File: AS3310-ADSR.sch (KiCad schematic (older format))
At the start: 51 parts

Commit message: Add Eurocad symbols and footprints.
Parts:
- added C? (x2): 10uF, symbol Device:C
- added J?: EURO_PWR_2x5, symbol eurorack:EURO_PWR_2x5
- added J?: ENVELOPE_OUT, symbol Connector:AudioJack2_Ground_SwitchT
- added TP?: GATE_IN, symbol Connector:TestPoint
- added TP?: TRIGGER_IN, symbol Connector:TestPoint
- added TP?: ENVELOPE_OUT, symbol Connector:TestPoint
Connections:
- net labels removed: ENVELOPE_OUT
- wire segments 123 -> 139
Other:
- note added: "Auto"
- note added: "Damp"
- note added: "Normal"
- moved on the sheet: C?, R?, U?

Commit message: Refactor
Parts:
- removed J?: EURO_PWR_2x5, symbol eurorack:EURO_PWR_2x5
- added C11, C8: .1uF, Seattle_Synths:C_Disc_D7.5mm_W2.5mm_P5.00mm, symbol Device:C
- added J2: EURO_PWR_2x5, Seattle_Synths:PinHeader_2x05_P2.54mm_Vertical, symbol Eurocad:EURO_PWR_2x5
- added unit 3 of U1
- C1, C10, C2, C3, C4, C5, C6, C7, C9: renamed from C?; footprint (none) -> Seattle_Synths:C_Disc_D7.5mm_W2.5mm_P5.00mm
- D1, D2: renamed from D?; footprint (none) -> Seattle_Synths:D_DO-35_SOD27_P7.62mm_Horizontal
- J1, J3, J4: renamed from J?; footprint (none) -> Seattle_Synths:Jack_3.5mm_QingPu_WQP-PJ398SM_Vertical_CircularHoles
- R1, R10, R11, R12, R13, R14, R15, R16, R17, R18, R19, R2, R20, R21, R22, R23, R24, R25, R3, R4, R5, R6, R7, R8, R9: renamed from R?; footprint (none) -> Seattle_Synths:R_Axial_DIN0207_L6.3mm_D2.5mm_P10.16mm_Horizontal
- RV1, RV2, RV3, RV4: renamed from RV?; footprint (none) -> Seattle_Synths:Potentiometer_Alpha_RD901F-40-00D_Single_Vertical
- RV5, RV6: renamed from RV?; footprint (none) -> Seattle_Synths:Potentiometer_Runtron_RM-065_Vertical
- SW2: renamed from SW?; footprint (none) -> Seattle_Synths:SW_PUSH_6mm_H5mm
- TP1, TP2, TP3: renamed from TP?; footprint (none) -> Seattle_Synths:TestPoint_Pad_4.0x4.0mm
- U1, U3, U4: renamed from U?; footprint (none) -> Seattle_Synths:DIP-8_W7.62mm
- U2: renamed from U?; footprint (none) -> Seattle_Synths:DIP-16_W7.62mm
- gave numbers to parts that had none: 3
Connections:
- wire segments 139 -> 141
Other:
- moved on the sheet: C10, C9

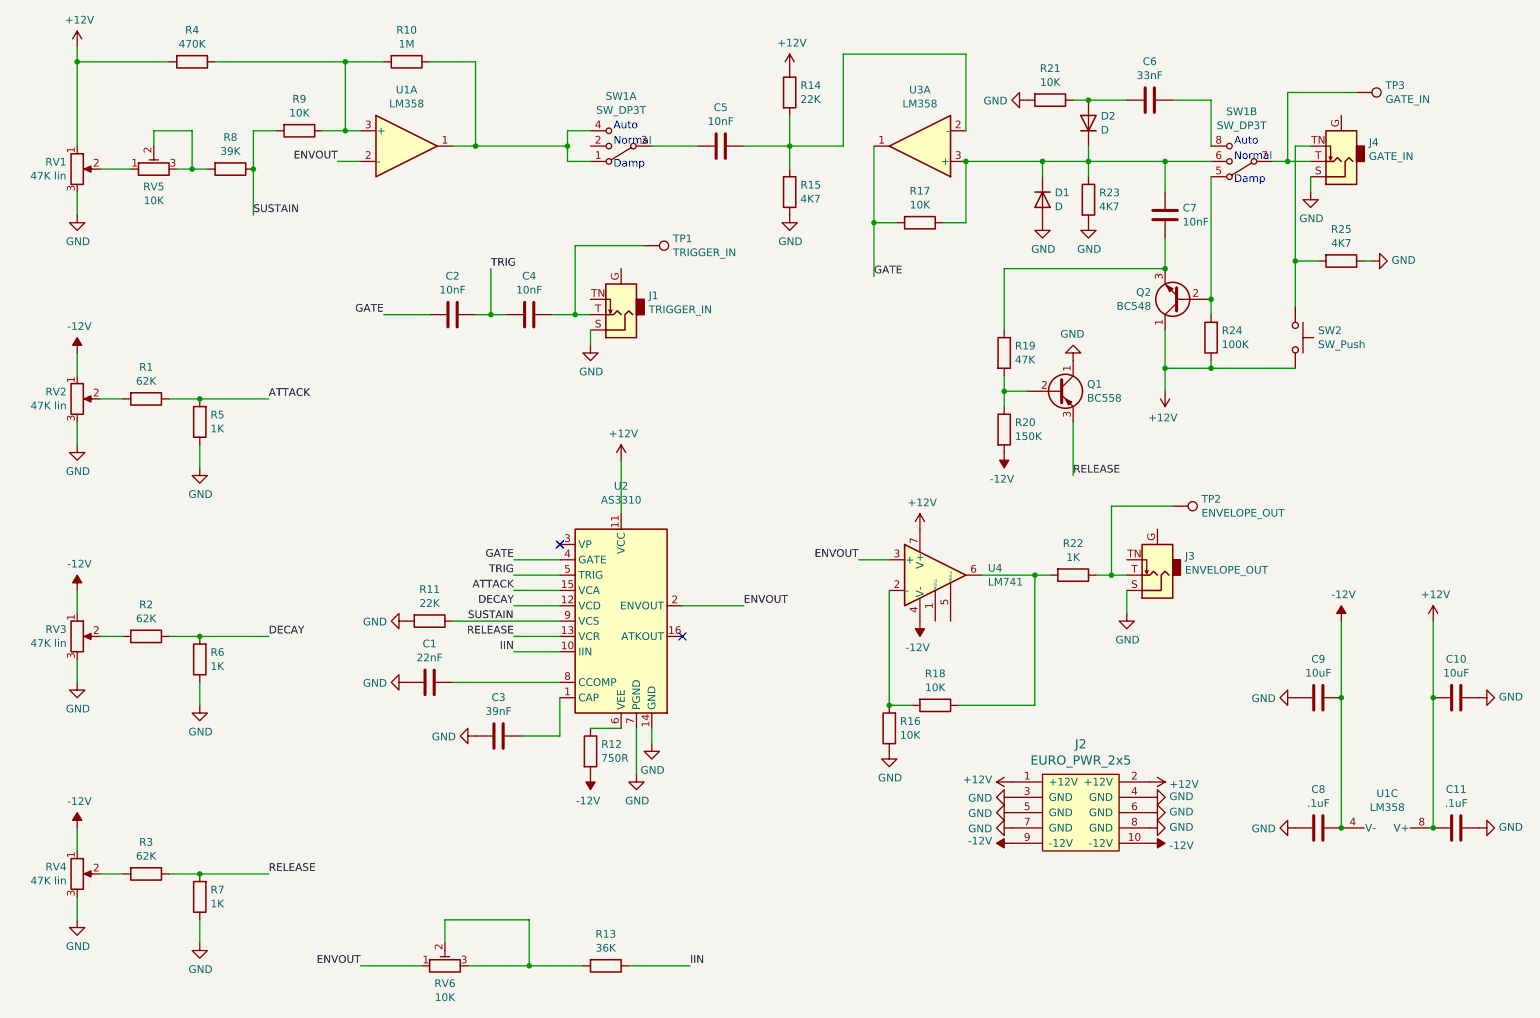
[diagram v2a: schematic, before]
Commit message: Refactor DP3T switch.
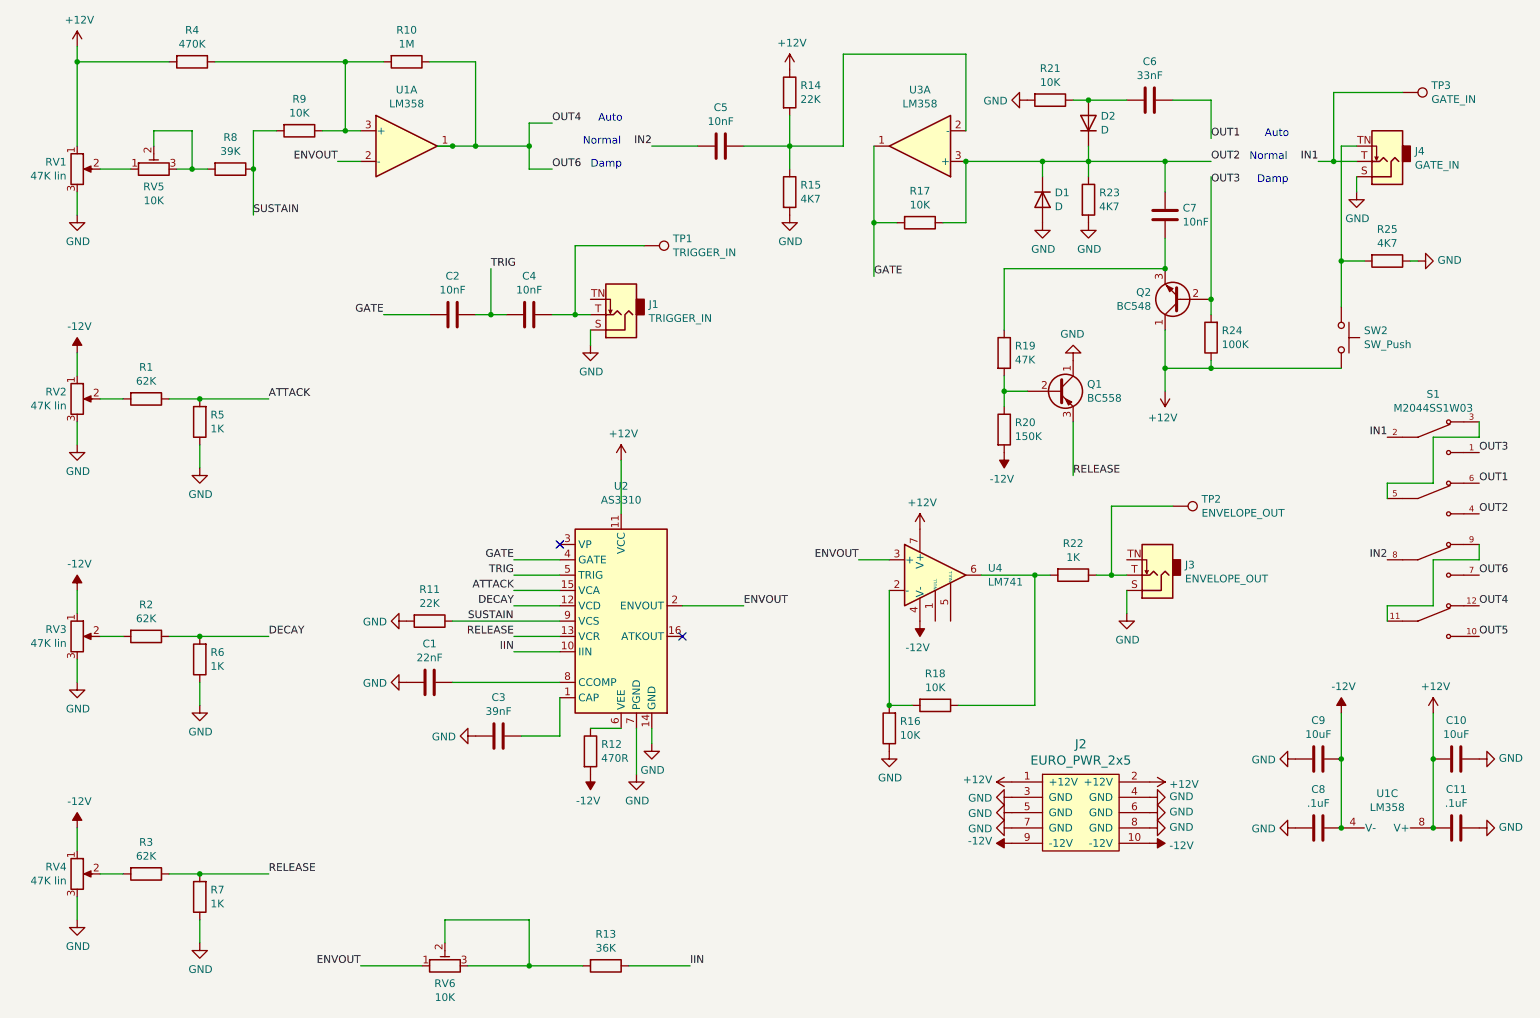
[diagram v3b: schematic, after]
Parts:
- removed J1: TRIGGER_IN, Seattle_Synths:Jack_3.5mm_QingPu_WQP-PJ398SM_Vertical_CircularHoles, symbol Connector:AudioJack2_Ground_SwitchT
- removed J3: ENVELOPE_OUT, Seattle_Synths:Jack_3.5mm_QingPu_WQP-PJ398SM_Vertical_CircularHoles, symbol Connector:AudioJack2_Ground_SwitchT
- removed J4: GATE_IN, Seattle_Synths:Jack_3.5mm_QingPu_WQP-PJ398SM_Vertical_CircularHoles, symbol Connector:AudioJack2_Ground_SwitchT
- removed SW1: SW_DP3T, symbol Switch:SW_DP3T
- added J1: TRIGGER_IN, Seattle_Synths:Jack_3.5mm_QingPu_WQP-PJ398SM_Vertical_CircularHoles, symbol Connector:AudioJack2_SwitchT
- added J3: ENVELOPE_OUT, Seattle_Synths:CUI_MJ-63052A, symbol Connector:AudioJack2_SwitchT
- added J4: GATE_IN, Seattle_Synths:Jack_3.5mm_QingPu_WQP-PJ398SM_Vertical_CircularHoles, symbol Connector:AudioJack2_SwitchT
- added S1: M2044SS1W03, Seattle_Synths:SW_M2044SS1W03, symbol Seattle_Synths_DP3T_Switch:M2044SS1W03
- R12: value 750R -> 470R
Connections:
- net GND: now also J1.S, J3.S, J4.S
- net OUT4: now reaches R10.1, U1.1
- net OUT4: now also S1.12, S1.7
- net IN2: now reaches C5.2
- net IN2: now also S1.8
- net OUT2: now reaches C7.1, D1.1 (K), D2.1 (K), R17.1, R23.1, U3.3 (+)
- net OUT2: now also S1.4
- net OUT1: now reaches C6.1
- net OUT1: now also S1.6
- net OUT3: now reaches Q2.2 (B), R24.2
- net OUT3: now also S1.1
- net at R25.2, SW2.1: now also J4.TN
- net at R22.1, TP2.1: now also J3.T
- net IN1: now reaches TP3.1
- net IN1: now also J4.T, S1.2
- net at C4.1, TP1.1: now also J1.T
- new net: S1.11, S1.9
- new net: S1.3, S1.5
- new net OUT5: S1.10
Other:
- moved on the sheet: C10, C9, R25, SW2, TP3

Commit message: Refactor
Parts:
- removed S1: M2044SS1W03, Seattle_Synths:SW_M2044SS1W03, symbol Seattle_Synths_DP3T_Switch:M2044SS1W03
- added D3: LED, symbol Device:LED
- added R26: 330R, symbol Device:R
- added S1: M2044SS1W03, SW_M2044SS1W03, symbol Seattle_Synths:M2044SS1W03
- added TP4: -12V, symbol Connector:TestPoint
- added TP5: GND, symbol Connector:TestPoint
- added TP6: +12V, symbol Connector:TestPoint
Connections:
- net +12V: now also R26.2, TP6.1
- net -12V: now also TP4.1
- net GND: now also D3.1 (K), TP5.1
- net IN1: now also S1.2
- net IN2: now also S1.8
- net OUT1: now also S1.6
- net OUT2: now also S1.4
- net OUT3: now also S1.1
- net OUT4: now also S1.12, S1.7
- net OUT5: now also S1.10
- new net: S1.11, S1.9
- new net: S1.3, S1.5
- new net: D3.2 (A), R26.1
- no-connect marks 2 -> 7
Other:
- moved on the sheet: C10, C11, C3, C8, C9, U1C

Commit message: Refacctor
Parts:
- D3: footprint (none) -> Seattle_Synths:LED_D5.0mm
- J3: footprint Seattle_Synths:CUI_MJ-63052A -> Seattle_Synths:Jack_3.5mm_QingPu_WQP-PJ398SM_Vertical_CircularHoles
- R26: footprint (none) -> Seattle_Synths:R_Axial_DIN0207_L6.3mm_D2.5mm_P10.16mm_Horizontal
- S1: footprint SW_M2044SS1W03 -> Seattle_Synths:SW_M2044SS1W03
- TP4, TP5, TP6: footprint (none) -> Seattle_Synths:TestPoint_Pad_4.0x4.0mm
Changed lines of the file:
@@
 F 0 "J3" H 8420 4433 50  0000 R CNN
 F 1 "ENVELOPE_OUT" H 8420 4524 50  0000 R CNN
-F 2 "Seattle_Synths:CUI_MJ-63052A" H 8600 4500 50  0001 C CNN
+F 2 "Seattle_Synths:Jack_3.5mm_QingPu_WQP-PJ398SM_Vertical_CircularHoles" H 8600 4500 50  0001 C CNN
 F 3 "~" H 8600 4500 50  0001 C CNN
 	1    8600 4500
@@
 F 0 "R26" V 5843 3300 50  0000 C CNN
 F 1 "330R" V 5934 3300 50  0000 C CNN
-F 2 "" V 5980 3300 50  0001 C CNN
+F 2 "Seattle_Synths:R_Axial_DIN0207_L6.3mm_D2.5mm_P10.16mm_Horizontal" V 5980 3300 50  0001 C CNN
 F 3 "~" H 6050 3300 50  0001 C CNN
 	1    6050 3300
@@
 F 0 "D3" H 6543 3045 50  0000 C CNN
 F 1 "LED" H 6543 3136 50  0000 C CNN
-F 2 "" H 6550 3300 50  0001 C CNN
+F 2 "Seattle_Synths:LED_D5.0mm" H 6550 3300 50  0001 C CNN
 F 3 "~" H 6550 3300 50  0001 C CNN
 	1    6550 3300
@@
 F 0 "S1" H 10450 4931 50  0000 C CNN
 F 1 "M2044SS1W03" H 10450 4840 50  0000 C CNN
-F 2 "SW_M2044SS1W03" H 10450 4050 50  0001 L BNN
+F 2 "Seattle_Synths:SW_M2044SS1W03" H 10450 4050 50  0001 L BNN
 F 3 "30.9 mm" H 10450 4050 50  0001 L BNN
 F 4 "NKK Switches" H 10450 4050 50  0001 L BNN "Field4"
@@
 F 0 "TP6" V 10204 5588 50  0000 L CNN
 F 1 "+12V" V 10295 5588 50  0000 L CNN
-F 2 "" H 10450 5400 50  0001 C CNN
+F 2 "Seattle_Synths:TestPoint_Pad_4.0x4.0mm" H 10450 5400 50  0001 C CNN
 F 3 "~" H 10450 5400 50  0001 C CNN
 	1    10250 5400
@@
 F 0 "TP4" V 9700 5650 50  0000 C CNN
 F 1 "-12V" V 9600 5700 50  0000 C CNN
-F 2 "" H 9850 5400 50  0001 C CNN
+F 2 "Seattle_Synths:TestPoint_Pad_4.0x4.0mm" H 9850 5400 50  0001 C CNN
 F 3 "~" H 9850 5400 50  0001 C CNN
 	1    9650 5400
@@
 F 0 "TP5" V 9900 5750 50  0000 R CNN
 F 1 "GND" V 9800 5750 50  0000 R CNN
-F 2 "" H 10150 5650 50  0001 C CNN
+F 2 "Seattle_Synths:TestPoint_Pad_4.0x4.0mm" H 10150 5650 50  0001 C CNN
 F 3 "~" H 10150 5650 50  0001 C CNN
 	1    9950 5650

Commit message: Refactor
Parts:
- removed C10, C9: 10uF, Seattle_Synths:C_Disc_D7.5mm_W2.5mm_P5.00mm, symbol Device:C
- added C10, C9: 10uF, Seattle_Synths:CP_Radial_D5.0mm_P2.50mm, symbol Device:C_Polarized
- RV5, RV6: footprint Seattle_Synths:Potentiometer_Runtron_RM-065_Vertical -> Seattle_Synths:TRIM_3266W-1-102LF
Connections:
- net +12V: now also C10.1
- net -12V: now also C9.2
- net GND: now also C10.2, C9.1
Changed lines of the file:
@@
 F 0 "RV5" V 1935 1850 50  0000 C CNN
 F 1 "10K" V 1844 1850 50  0000 C CNN
-F 2 "Seattle_Synths:Potentiometer_Runtron_RM-065_Vertical" H 2050 1850 50  0001 C CNN
+F 2 "Seattle_Synths:TRIM_3266W-1-102LF" H 2050 1850 50  0001 C CNN
 F 3 "~" H 2050 1850 50  0001 C CNN
 	1    2050 1850
@@
 F 0 "RV6" V 3835 7050 50  0000 C CNN
 F 1 "10K" V 3744 7050 50  0000 C CNN
-F 2 "Seattle_Synths:Potentiometer_Runtron_RM-065_Vertical" H 3950 7050 50  0001 C CNN
+F 2 "Seattle_Synths:TRIM_3266W-1-102LF" H 3950 7050 50  0001 C CNN
 F 3 "~" H 3950 7050 50  0001 C CNN
 	1    3950 7050
@@
 $EndComp
 $Comp
-L Device:C C10
-U 1 1 5FA29AF6
-P 10400 5800
-F 0 "C10" V 10652 5800 50  0000 C CNN
-F 1 "10uF" V 10561 5800 50  0000 C CNN
-F 2 "Seattle_Synths:C_Disc_D7.5mm_W2.5mm_P5.00mm" H 10438 5650 50  0001 C CNN
-F 3 "~" H 10400 5800 50  0001 C CNN
-	1    10400 5800
-	0    -1   -1   0
-$EndComp
-$Comp
-L Device:C C9
-U 1 1 5FA2971B
-P 9500 5800
-F 0 "C9" V 9752 5800 50  0000 C CNN
-F 1 "10uF" V 9661 5800 50  0000 C CNN
-F 2 "Seattle_Synths:C_Disc_D7.5mm_W2.5mm_P5.00mm" H 9538 5650 50  0001 C CNN
-F 3 "~" H 9500 5800 50  0001 C CNN
-	1    9500 5800
-	0    -1   -1   0
-$EndComp
-$Comp
 L Connector:TestPoint TP6
 U 1 1 5FD53960
@@
 	-1   0    0    1
 $EndComp
+$Comp
+L Device:C_Polarized C9
+U 1 1 5FA9F7E0
+P 9500 5800
+F 0 "C9" V 9755 5800 50  0000 C CNN
+F 1 "10uF" V 9664 5800 50  0000 C CNN
+F 2 "Seattle_Synths:CP_Radial_D5.0mm_P2.50mm" H 9538 5650 50  0001 C CNN
+F 3 "~" H 9500 5800 50  0001 C CNN
+	1    9500 5800
+	0    -1   -1   0
+$EndComp
+$Comp
+L Device:C_Polarized C10
+U 1 1 5FAA7021
+P 10400 5800
+F 0 "C10" V 10655 5800 50  0000 C CNN
+F 1 "10uF" V 10564 5800 50  0000 C CNN
+F 2 "Seattle_Synths:CP_Radial_D5.0mm_P2.50mm" H 10438 5650 50  0001 C CNN
+F 3 "~" H 10400 5800 50  0001 C CNN
+	1    10400 5800
+	0    -1   -1   0
+$EndComp
 $EndSCHEMATC

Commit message: Refactor
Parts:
- SW2: footprint Seattle_Synths:SW_PUSH_6mm_H5mm -> Seattle_Synths:SW_PS1024ALRED
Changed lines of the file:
@@
 F 0 "SW2" V 9754 3098 50  0000 L CNN
 F 1 "SW_Push" V 9845 3098 50  0000 L CNN
-F 2 "Seattle_Synths:SW_PUSH_6mm_H5mm" H 9800 3150 50  0001 C CNN
+F 2 "Seattle_Synths:SW_PS1024ALRED" H 9800 3150 50  0001 C CNN
 F 3 "~" H 9800 3150 50  0001 C CNN
 	1    9800 2950
